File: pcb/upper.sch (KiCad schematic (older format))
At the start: 16 parts, among them J101 MALE, J102 FEMALE, J103 MALE, J104 FEMALE, J105 MALE, J106 FEMALE, J107 MALE, J108 FEMALE, J111 STANDOFF, J112 STANDOFF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

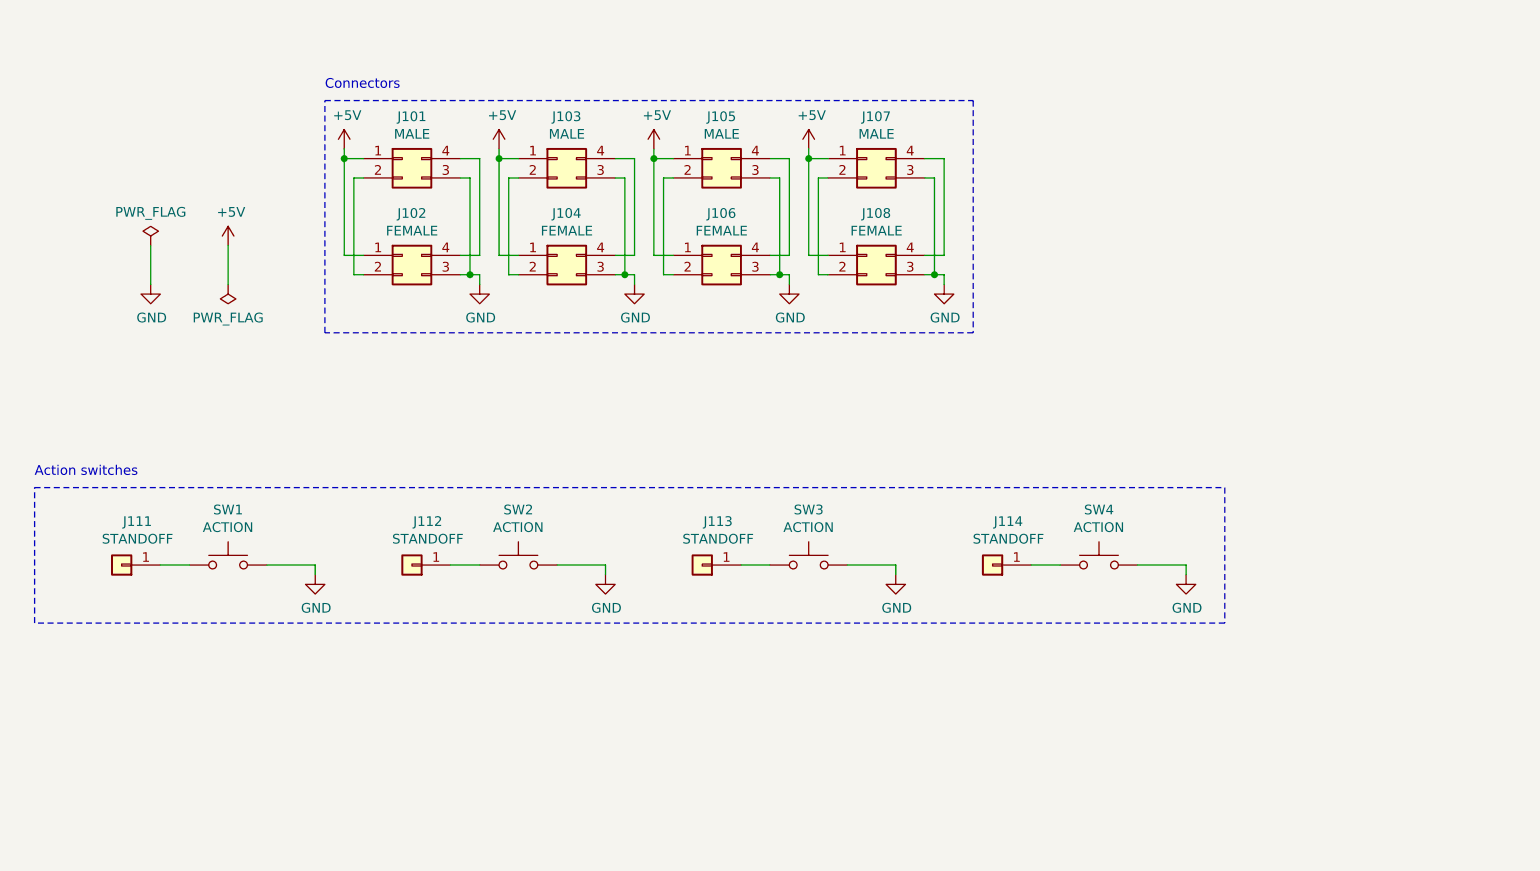
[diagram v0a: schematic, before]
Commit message: Fix: Wrong pin order in upper board
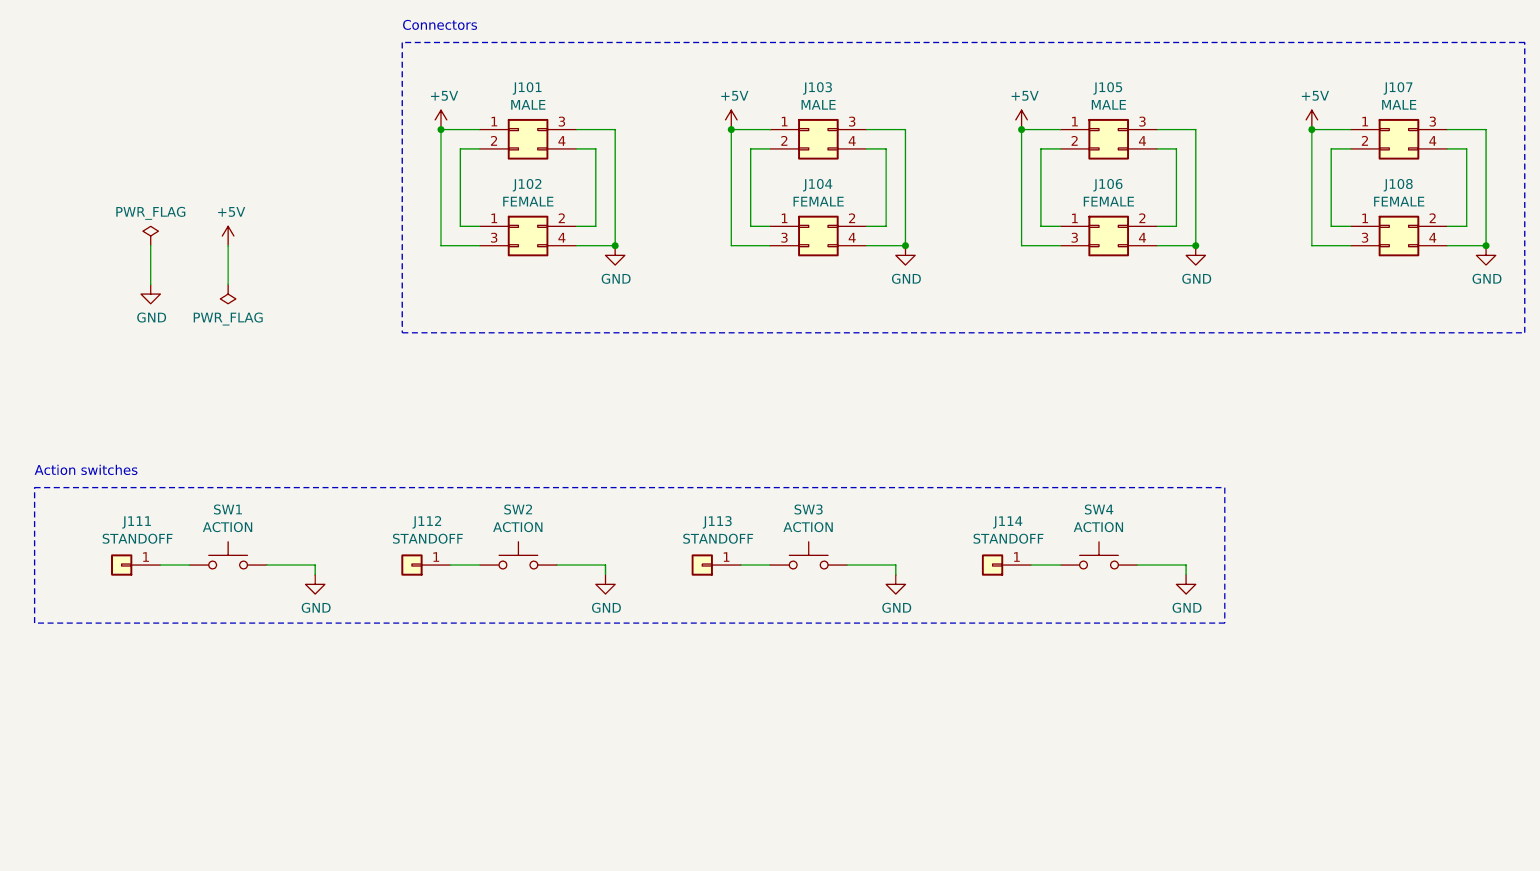
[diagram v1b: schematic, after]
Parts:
- removed J101, J103, J105, J107: MALE, Connector_PinHeader_2.54mm:PinHeader_2x02_P2.54mm_Horizontal, symbol Connector_Generic:Conn_02x02_Counter_Clockwise
- removed J102, J104, J106, J108: FEMALE, Connector_PinSocket_2.54mm:PinSocket_2x02_P2.54mm_Horizontal, symbol Connector_Generic:Conn_02x02_Counter_Clockwise
- added J101, J103, J105, J107: MALE, Connector_PinHeader_2.54mm:PinHeader_2x02_P2.54mm_Horizontal, symbol Connector_Generic:Conn_02x02_Top_Bottom
- added J102, J104, J106, J108: FEMALE, Connector_PinSocket_2.54mm:PinSocket_2x02_P2.54mm_Horizontal, symbol Connector_Generic:Conn_02x02_Odd_Even
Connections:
- net +5V: now also J101.1 (Pin_1), J102.3 (Pin_3), J103.1 (Pin_1), J104.3 (Pin_3), J105.1 (Pin_1), J106.3 (Pin_3), J107.1 (Pin_1), J108.3 (Pin_3)
- net GND: now also J101.3 (Pin_3), J102.4 (Pin_4), J103.3 (Pin_3), J104.4 (Pin_4), J105.3 (Pin_3), J106.4 (Pin_4), J107.3 (Pin_3), J108.4 (Pin_4)
- new net: J101.2 (Pin_2), J102.1 (Pin_1)
- new net: J101.4 (Pin_4), J102.2 (Pin_2)
- new net: J107.2 (Pin_2), J108.1 (Pin_1)
- new net: J107.4 (Pin_4), J108.2 (Pin_2)
- new net: J103.2 (Pin_2), J104.1 (Pin_1)
- new net: J103.4 (Pin_4), J104.2 (Pin_2)
- new net: J105.2 (Pin_2), J106.1 (Pin_1)
- new net: J105.4 (Pin_4), J106.2 (Pin_2)

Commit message: Fix: UIDs of connectors changed
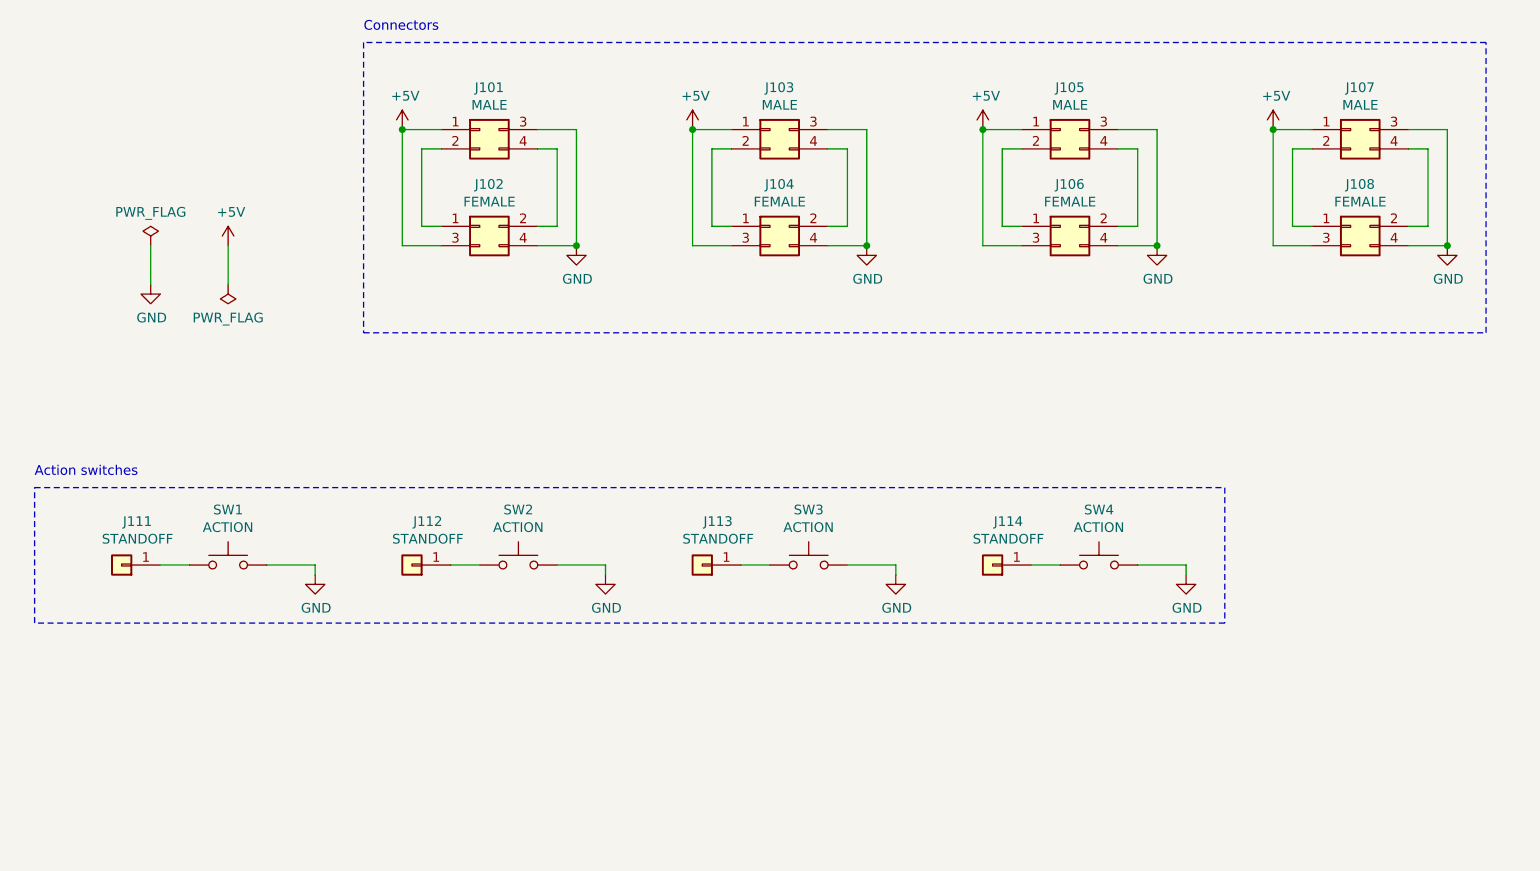
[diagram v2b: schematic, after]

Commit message: Make fields compatible with JLCPCB BOM plugin
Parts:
- J101, J103, J105, J107: JLCPCB BOM (none) -> False; LCSC Part (none) -> C239333; LCSC Part # C239333 -> (none)
- J102, J104, J106, J108: JLCPCB BOM (none) -> False; LCSC Part (none) -> C239353; LCSC Part # C239353 -> (none)
- J111, J112, J113, J114: JLCPCB BOM (none) -> False
- SW1, SW2, SW3, SW4: LCSC Part (none) -> C318884; LCSC Part # C318884 -> (none)
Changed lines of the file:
@@
 F 2 "node:top-leaf" H 2900 4400 50  0001 C CNN
 F 3 "https://datasheet.lcsc.com/szlcsc/2002271431_XKB-Connectivity-TS-1187A-B-A-B_C318884.pdf" H 2900 4400 50  0001 C CNN
-F 4 "C318884" H 2900 4200 50  0001 C CNN "LCSC Part #"
+F 4 "C318884" H 2900 4200 50  0001 C CNN "LCSC Part"
 F 5 "TS-1187A-B-A-B" H 2900 4200 50  0001 C CNN "MPN"
 F 6 "XKB Connectivity" H 2900 4200 50  0001 C CNN "Manufacturer"
@@
 F 2 "node:top-leaf" H 4400 4400 50  0001 C CNN
 F 3 "https://datasheet.lcsc.com/szlcsc/2002271431_XKB-Connectivity-TS-1187A-B-A-B_C318884.pdf" H 4400 4400 50  0001 C CNN
-F 4 "C318884" H 4400 4200 50  0001 C CNN "LCSC Part #"
+F 4 "C318884" H 4400 4200 50  0001 C CNN "LCSC Part"
 F 5 "TS-1187A-B-A-B" H 4400 4200 50  0001 C CNN "MPN"
 F 6 "XKB Connectivity" H 4400 4200 50  0001 C CNN "Manufacturer"
@@
 F 2 "node:top-leaf" H 5900 4400 50  0001 C CNN
 F 3 "https://datasheet.lcsc.com/szlcsc/2002271431_XKB-Connectivity-TS-1187A-B-A-B_C318884.pdf" H 5900 4400 50  0001 C CNN
-F 4 "C318884" H 5900 4200 50  0001 C CNN "LCSC Part #"
+F 4 "C318884" H 5900 4200 50  0001 C CNN "LCSC Part"
 F 5 "TS-1187A-B-A-B" H 5900 4200 50  0001 C CNN "MPN"
 F 6 "XKB Connectivity" H 5900 4200 50  0001 C CNN "Manufacturer"
@@
 F 2 "node:top-leaf" H 7400 4400 50  0001 C CNN
 F 3 "https://datasheet.lcsc.com/szlcsc/2002271431_XKB-Connectivity-TS-1187A-B-A-B_C318884.pdf" H 7400 4400 50  0001 C CNN
-F 4 "C318884" H 7400 4200 50  0001 C CNN "LCSC Part #"
+F 4 "C318884" H 7400 4200 50  0001 C CNN "LCSC Part"
 F 5 "TS-1187A-B-A-B" H 7400 4200 50  0001 C CNN "MPN"
 F 6 "XKB Connectivity" H 7400 4200 50  0001 C CNN "Manufacturer"
@@
 F 2 "MountingHole:MountingHole_2.2mm_M2_Pad_Via" H 2350 4200 50  0001 C CNN
 F 3 "~" H 2350 4200 50  0001 C CNN
+F 4 "False" H 2350 4200 50  0001 C CNN "JLCPCB BOM"
 	1    2350 4200
 	-1   0    0    1
@@
 F 2 "MountingHole:MountingHole_2.2mm_M2_Pad_Via" H 3850 4200 50  0001 C CNN
 F 3 "~" H 3850 4200 50  0001 C CNN
+F 4 "False" H 3850 4200 50  0001 C CNN "JLCPCB BOM"
 	1    3850 4200
 	-1   0    0    1
@@
 F 2 "MountingHole:MountingHole_2.2mm_M2_Pad_Via" H 5350 4200 50  0001 C CNN
 F 3 "~" H 5350 4200 50  0001 C CNN
+F 4 "False" H 5350 4200 50  0001 C CNN "JLCPCB BOM"
 	1    5350 4200
 	-1   0    0    1
@@
 F 2 "MountingHole:MountingHole_2.2mm_M2_Pad_Via" H 6850 4200 50  0001 C CNN
 F 3 "~" H 6850 4200 50  0001 C CNN
+F 4 "False" H 6850 4200 50  0001 C CNN "JLCPCB BOM"
 	1    6850 4200
 	-1   0    0    1
@@
 F 2 "Connector_PinSocket_2.54mm:PinSocket_2x02_P2.54mm_Horizontal" H 8700 2450 50  0001 C CNN
 F 3 "https://datasheet.lcsc.com/szlcsc/2008120038_CJT-Changjiang-Connectors-A2541HWR-2x2P_C239353.pdf" H 8700 2450 50  0001 C CNN
-F 4 "C239353" H 8700 2450 50  0001 C CNN "LCSC Part #"
+F 4 "C239353" H 8700 2450 50  0001 C CNN "LCSC Part"
 F 5 "A2541HWR-2x2P" H 8700 2450 50  0001 C CNN "MPN"
 F 6 "CJT(Changjiang Connectors)" H 8700 2450 50  0001 C CNN "Manufacturer"
+F 7 "False" H 8700 2450 50  0001 C CNN "JLCPCB BOM"
 	1    8700 2450
 	1    0    0    -1
@@
 F 2 "Connector_PinHeader_2.54mm:PinHeader_2x02_P2.54mm_Horizontal" H 8700 1950 50  0001 C CNN
 F 3 "https://datasheet.lcsc.com/szlcsc/2008120037_CJT-Changjiang-Connectors-A2541WR-2x2P_C239333.pdf" H 8700 1950 50  0001 C CNN
-F 4 "C239333" H 8700 1950 50  0001 C CNN "LCSC Part #"
+F 4 "C239333" H 8700 1950 50  0001 C CNN "LCSC Part"
 F 5 "A2541WR-2x2P" H 8700 1950 50  0001 C CNN "MPN"
 F 6 "CJT(Changjiang Connectors)" H 8700 1950 50  0001 C CNN "Manufacturer"
+F 7 "False" H 8700 1950 50  0001 C CNN "JLCPCB BOM"
 	1    8700 1950
 	1    0    0    -1
@@
 F 2 "Connector_PinSocket_2.54mm:PinSocket_2x02_P2.54mm_Horizontal" H 7200 2450 50  0001 C CNN
 F 3 "https://datasheet.lcsc.com/szlcsc/2008120038_CJT-Changjiang-Connectors-A2541HWR-2x2P_C239353.pdf" H 7200 2450 50  0001 C CNN
-F 4 "C239353" H 7200 2450 50  0001 C CNN "LCSC Part #"
+F 4 "C239353" H 7200 2450 50  0001 C CNN "LCSC Part"
 F 5 "A2541HWR-2x2P" H 7200 2450 50  0001 C CNN "MPN"
 F 6 "CJT(Changjiang Connectors)" H 7200 2450 50  0001 C CNN "Manufacturer"
+F 7 "False" H 7200 2450 50  0001 C CNN "JLCPCB BOM"
 	1    7200 2450
 	1    0    0    -1
@@
 F 2 "Connector_PinHeader_2.54mm:PinHeader_2x02_P2.54mm_Horizontal" H 7200 1950 50  0001 C CNN
 F 3 "https://datasheet.lcsc.com/szlcsc/2008120037_CJT-Changjiang-Connectors-A2541WR-2x2P_C239333.pdf" H 7200 1950 50  0001 C CNN
-F 4 "C239333" H 7200 1950 50  0001 C CNN "LCSC Part #"
+F 4 "C239333" H 7200 1950 50  0001 C CNN "LCSC Part"
 F 5 "A2541WR-2x2P" H 7200 1950 50  0001 C CNN "MPN"
 F 6 "CJT(Changjiang Connectors)" H 7200 1950 50  0001 C CNN "Manufacturer"
+F 7 "False" H 7200 1950 50  0001 C CNN "JLCPCB BOM"
 	1    7200 1950
 	1    0    0    -1
@@
 F 2 "Connector_PinSocket_2.54mm:PinSocket_2x02_P2.54mm_Horizontal" H 5700 2450 50  0001 C CNN
 F 3 "https://datasheet.lcsc.com/szlcsc/2008120038_CJT-Changjiang-Connectors-A2541HWR-2x2P_C239353.pdf" H 5700 2450 50  0001 C CNN
-F 4 "C239353" H 5700 2450 50  0001 C CNN "LCSC Part #"
+F 4 "C239353" H 5700 2450 50  0001 C CNN "LCSC Part"
 F 5 "A2541HWR-2x2P" H 5700 2450 50  0001 C CNN "MPN"
 F 6 "CJT(Changjiang Connectors)" H 5700 2450 50  0001 C CNN "Manufacturer"
+F 7 "False" H 5700 2450 50  0001 C CNN "JLCPCB BOM"
 	1    5700 2450
 	1    0    0    -1
@@
 F 2 "Connector_PinHeader_2.54mm:PinHeader_2x02_P2.54mm_Horizontal" H 5700 1950 50  0001 C CNN
 F 3 "https://datasheet.lcsc.com/szlcsc/2008120037_CJT-Changjiang-Connectors-A2541WR-2x2P_C239333.pdf" H 5700 1950 50  0001 C CNN
-F 4 "C239333" H 5700 1950 50  0001 C CNN "LCSC Part #"
+F 4 "C239333" H 5700 1950 50  0001 C CNN "LCSC Part"
 F 5 "A2541WR-2x2P" H 5700 1950 50  0001 C CNN "MPN"
 F 6 "CJT(Changjiang Connectors)" H 5700 1950 50  0001 C CNN "Manufacturer"
+F 7 "False" H 5700 1950 50  0001 C CNN "JLCPCB BOM"
 	1    5700 1950
 	1    0    0    -1
@@
 F 2 "Connector_PinHeader_2.54mm:PinHeader_2x02_P2.54mm_Horizontal" H 4200 1950 50  0001 C CNN
 F 3 "https://datasheet.lcsc.com/szlcsc/2008120037_CJT-Changjiang-Connectors-A2541WR-2x2P_C239333.pdf" H 4200 1950 50  0001 C CNN
-F 4 "C239333" H 4200 1950 50  0001 C CNN "LCSC Part #"
+F 4 "C239333" H 4200 1950 50  0001 C CNN "LCSC Part"
 F 5 "A2541WR-2x2P" H 4200 1950 50  0001 C CNN "MPN"
 F 6 "CJT(Changjiang Connectors)" H 4200 1950 50  0001 C CNN "Manufacturer"
+F 7 "False" H 4200 1950 50  0001 C CNN "JLCPCB BOM"
 	1    4200 1950
 	1    0    0    -1
@@
 F 2 "Connector_PinSocket_2.54mm:PinSocket_2x02_P2.54mm_Horizontal" H 4200 2450 50  0001 C CNN
 F 3 "https://datasheet.lcsc.com/szlcsc/2008120038_CJT-Changjiang-Connectors-A2541HWR-2x2P_C239353.pdf" H 4200 2450 50  0001 C CNN
-F 4 "C239353" H 4200 2450 50  0001 C CNN "LCSC Part #"
+F 4 "C239353" H 4200 2450 50  0001 C CNN "LCSC Part"
 F 5 "A2541HWR-2x2P" H 4200 2450 50  0001 C CNN "MPN"
 F 6 "CJT(Changjiang Connectors)" H 4200 2450 50  0001 C CNN "Manufacturer"
+F 7 "False" H 4200 2450 50  0001 C CNN "JLCPCB BOM"
 	1    4200 2450
 	1    0    0    -1
